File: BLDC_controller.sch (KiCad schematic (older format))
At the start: 77 parts, among them P1 CONN_01X02, P2 CONN_01X04, P3 CONN_01X02, P4 CONN_01X03, Q1 PSMN2R0-30YLD, Q2 PSMN2R0-30YLD, Q3 PSMN2R0-30YLD, Q4 PSMN2R0-30YLD, Q5 PSMN2R0-30YLD, Q6 PSMN2R0-30YLD

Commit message: add HALL header
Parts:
- added C18, C19: 220u, symbol CP
- added C20: 22u, symbol CP
- added C21: 10u, symbol CP
- added C22, C23, C24: 10p, symbol C
- added P5: CONN_01X05, symbol CONN_01X05
- added R40: 2k2, project_footprints:R_0603, symbol R
- added R41, R42, R43: 1k0, symbol R
- added R44, R45, R46: 10k, symbol R
- added V10: LED_ALT, symbol LED_ALT
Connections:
- wire segments 218 -> 257
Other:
- moved on the sheet: C15, C17, C7, L1, P1, R36, R37, R38, V8, V9

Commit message: minor change
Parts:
- removed C21: 10u, symbol CP
- removed P3: CONN_01X02, symbol CONN_01X02
- added P?: CONN_01X03, symbol CONN_01X03
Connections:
- wire segments 257 -> 252
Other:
- moved on the sheet: C10, C11, C12, C22, C23, C24, C9, P5, R17, R18, R19, R20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

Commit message: minor corrections
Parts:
- removed P2: CONN_01X04, symbol CONN_01X04
- added P2: CONN_01X06, symbol CONN_01X06
- added R47, R48, R49, R50: 1k0, project_footprints:R_0603, symbol R
- C22, C23, C24: footprint (none) -> project_footprints:C_0603
- R41, R42, R43, R44, R45, R46: footprint (none) -> project_footprints:R_0603
- gave numbers to parts that had none: 1
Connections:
- net labels added: 12V_FB, FP0, FP1, HALL1/A+, HALL2/B+, HALL3/Z+, I2C_SCL, I2C_SDA, NRST, OC_COMP, SW, SWCLK, SWDIO
- net labels removed: UART1_RX, UART1_TX
- wire segments 252 -> 259
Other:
- note added: "Digital\nHALL sensors"
- note added: "FP[1:0] determines \nA[1:0] of the I2C address"
- note added: "ST-LINK"
- moved on the sheet: C1, C10, C11, C12, C13, C14, C15, C16, C17, C18, C19, C2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

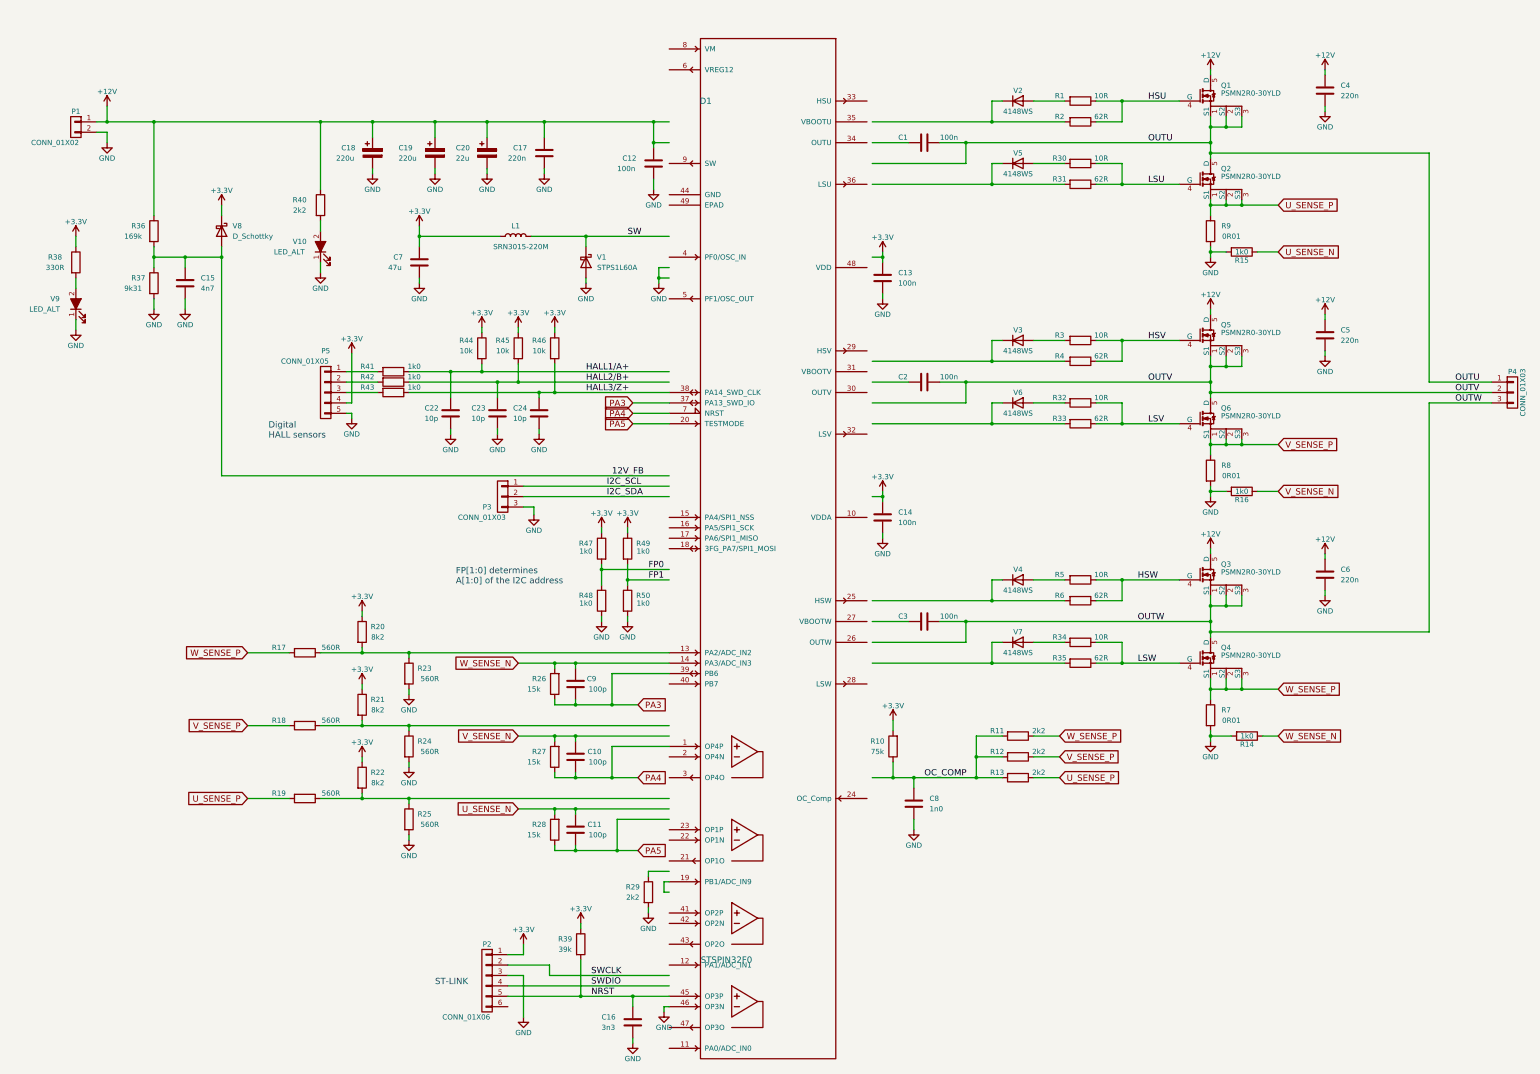
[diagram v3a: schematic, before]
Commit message: add SPI interface
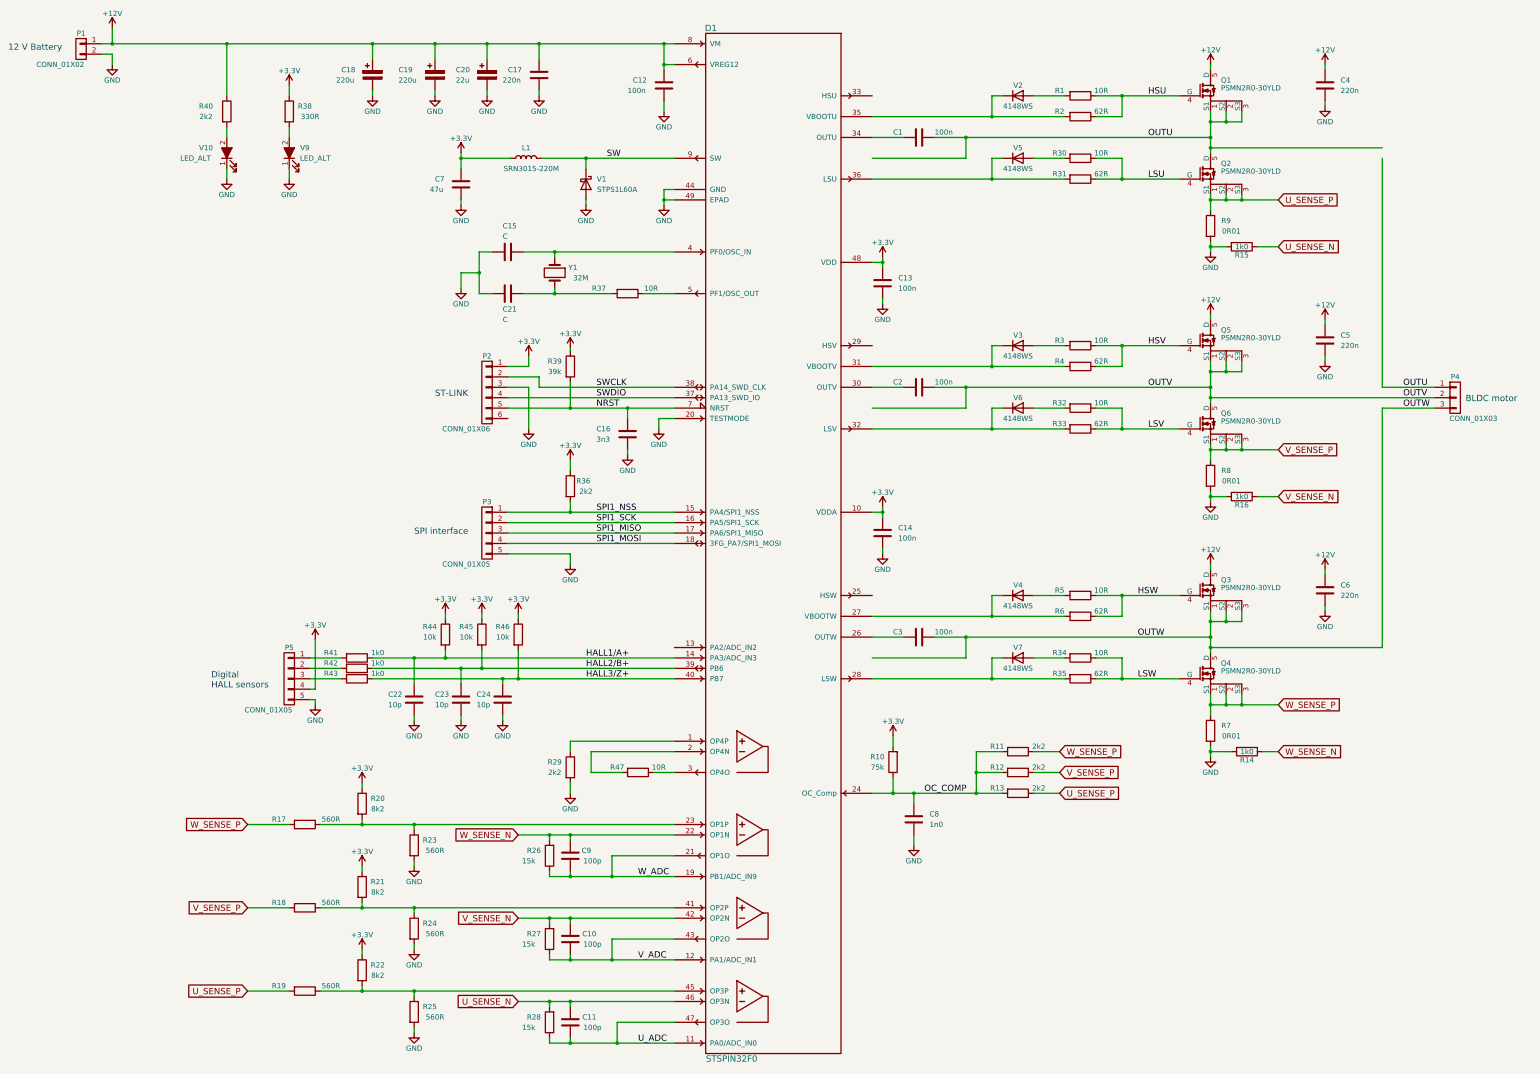
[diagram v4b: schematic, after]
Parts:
- removed P3: CONN_01X03, symbol CONN_01X03
- removed R48, R49, R50: 1k0, project_footprints:R_0603, symbol R
- removed V8: D_Schottky, symbol D_Schottky
- added C21: C, symbol C
- added P3: CONN_01X05, symbol CONN_01X05
- added Y1: 32M, symbol Crystal
- C15: value 4n7 -> C; footprint project_footprints:C_0603 -> (none)
- R36: value 169k -> 2k2; footprint project_footprints:R_0603 -> (none)
- R37: value 9k31 -> 10R; footprint project_footprints:R_0603 -> (none)
- R47: value 1k0 -> 10R
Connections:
- net labels added: SPI1_MISO, SPI1_MOSI, SPI1_NSS, SPI1_SCK, U_ADC, V_ADC, W_ADC
- net labels removed: 12V_FB, FP0, FP1, I2C_SCL, I2C_SDA, PA3, PA4, PA5
- wire segments 259 -> 254
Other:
- note added: "12 V Battery"
- note added: "BLDC motor"
- note added: "SPI interface"
- note removed: "FP[1:0] determines \nA[1:0] of the I2C address"
- moved on the sheet: C1, C10, C11, C12, C13, C14, C16, C17, C18, C19, C2, C20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

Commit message: cosmetic changes
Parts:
- C15, C21, R37: footprint (none) -> project_footprints:C_0603
- R36: footprint (none) -> project_footprints:R_0603
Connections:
- net OUTU: now also D1.34 (OUTU)
- net OUTV: now also D1.30 (OUTV)
- net OUTW: now also D1.26 (OUTW)
- net at D1.25 (HSW): now also R6.2, V4.1 (K)
- net at C3.2: now also D1.27 (VBOOTW); no longer D1.26 (OUTW)
- net at D1.29 (HSV): now also R4.2, V3.1 (K)
- net at C2.2: now also D1.31 (VBOOTV); no longer D1.30 (OUTV)
- net at D1.33 (HSU): now also R2.2, V2.1 (K)
- net at C1.2: now also D1.35 (VBOOTU); no longer D1.34 (OUTU)
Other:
- note added: "2816: 2 W @ +70 C"
- note added: "AN4999 Application note - STSPIN32F0 overcurrent protection:\n\nOC_TH_STBY2 (PF6) = 0\nOC_TH_STBY1 (PF7) = 1\nOC_SEL (PA11) = 1\nOC threshold = 100 mV"
- moved on the sheet: C1, C2, C3, C4, C5, C6, Q1, Q2, Q3, Q4, Q5, Q6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

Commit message: overcurrent protection documented
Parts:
- R10: value 75k -> 46k4
- R7, R8, R9: footprint project_footprints:R_2816 -> project_footprints:R_2512
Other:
- note added: "15 A current through a sense resistor causes 2.25 W heat dissipation. \nHowever, none of the three sense resistor conducts 100% of the time."
- note added: "AN2868 Application note - Oscillator design guide for STM32"
- note added: "AN4999 Application note - STSPIN32F0 overcurrent protection:\n\nOC_TH_STBY2 (PF6) = 0\nOC_TH_STBY1 (PF7) = 1\nOC_SEL (PA11) = 1\nOC threshold = 100 mV\n\nImax = 14.6 A => R10 = 46k4\n\nC8 = 1 nF => f_LP = 220 kHz\nwhich is about 5.5 times the switching frequency\n"
- note added: "Bourns CRA2512-FZ-R010ELF\n2512: 3 W @ +70 C"
- note removed: "2816: 2 W @ +70 C"
- note removed: "AN4999 Application note - STSPIN32F0 overcurrent protection:\n\nOC_TH_STBY2 (PF6) = 0\nOC_TH_STBY1 (PF7) = 1\nOC_SEL (PA11) = 1\nOC threshold = 100 mV"

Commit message: most footprints selected
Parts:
- removed Y1: 32M, symbol Crystal
- added G1: NX3225GD, project_footprints:Crystal_3225, symbol Crystal
- C18, C19: footprint (none) -> project_footprints:C_Radial_D10_L25_P5
- P2: footprint (none) -> project_footprints:PINHEAD1-6
- P3, P5: footprint (none) -> project_footprints:PINHEAD1-5
- V10, V9: footprint (none) -> project_footprints:LED_0402
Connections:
- net OSC_IN: now reaches C15.1, D1.4 (PF0/OSC_IN)
- net OSC_IN: now also G1.1
- net at C21.1, R37.2: now also G1.2
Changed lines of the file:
@@
 Sheet 1 1
 Title "BLDC CONTROLLER"
-Date "18.02.2017"
+Date "19.02.2017"
 Rev "0.2"
 Comp "Helsinki Hacklab"
@@
 F 0 "V9" V 3750 2000 50  0000 C CNN
 F 1 "LED_ALT" V 3650 1900 50  0000 C CNN
-F 2 "" H 3700 2150 50  0001 C CNN
+F 2 "project_footprints:LED_0402" H 3700 2150 50  0001 C CNN
 F 3 "" H 3700 2150 50  0000 C CNN
 	1    3700 2150
@@
 F 0 "C18" H 4200 1450 50  0000 L CNN
 F 1 "220u" H 4150 1350 50  0000 L CNN
-F 2 "" H 4538 1250 50  0001 C CNN
+F 2 "project_footprints:C_Radial_D10_L25_P5" H 4538 1250 50  0001 C CNN
 F 3 "" H 4500 1400 50  0000 C CNN
 	1    4500 1400
@@
 F 0 "C19" H 4750 1450 50  0000 L CNN
 F 1 "220u" H 4750 1350 50  0000 L CNN
-F 2 "" H 5138 1250 50  0001 C CNN
+F 2 "project_footprints:C_Radial_D10_L25_P5" H 5138 1250 50  0001 C CNN
 F 3 "" H 5100 1400 50  0000 C CNN
 	1    5100 1400
@@
 F 0 "V10" V 3150 2350 50  0000 C CNN
 F 1 "LED_ALT" V 3050 2450 50  0000 C CNN
-F 2 "" H 3100 2150 50  0001 C CNN
+F 2 "project_footprints:LED_0402" H 3100 2150 50  0001 C CNN
 F 3 "" H 3100 2150 50  0000 C CNN
 	1    3100 2150
@@
 F 0 "P5" H 3700 7500 50  0000 C CNN
 F 1 "CONN_01X05" H 3900 6900 50  0000 C CNN
-F 2 "" H 3700 7200 50  0001 C CNN
+F 2 "project_footprints:PINHEAD1-5" H 3700 7200 50  0001 C CNN
 F 3 "" H 3700 7200 50  0000 C CNN
 	1    3700 7200
@@
 F 0 "P2" H 5600 4800 50  0000 C CNN
 F 1 "CONN_01X06" H 5800 4100 50  0000 C CNN
-F 2 "" H 5600 4450 50  0001 C CNN
+F 2 "project_footprints:PINHEAD1-6" H 5600 4450 50  0001 C CNN
 F 3 "" H 5600 4450 50  0000 C CNN
 	1    5600 4450
@@
 	1    0    0    -1
 $EndComp
-$Comp
-L Crystal Y1
-U 1 1 58AA45EE
-P 6250 3300
-F 0 "Y1" V 6200 3475 50  0000 C CNN
-F 1 "32M" V 6300 3550 50  0000 C CNN
-F 2 "" H 6250 3300 50  0001 C CNN
-F 3 "" H 6250 3300 50  0000 C CNN
-	1    6250 3300
-	0    1    1    0
-$EndComp
 Wire Wire Line
 	6250 3150 6250 3100
@@
 F 0 "P3" H 5600 6100 50  0000 C CNN
 F 1 "CONN_01X05" H 5800 5500 50  0000 C CNN
-F 2 "" H 5600 5800 50  0001 C CNN
+F 2 "project_footprints:PINHEAD1-5" H 5600 5800 50  0001 C CNN
 F 3 "" H 5600 5800 50  0000 C CNN
 	1    5600 5800
@@
 Text Notes 2150 3200 0    60   ~ 0
 AN2868 Application note - Oscillator design guide for STM32
+Text Label 6800 3100 0    60   ~ 0
+OSC_IN
+$Comp
+L Crystal G1
+U 1 1 58AD39C7
+P 6250 3300
+F 0 "G1" V 6200 3500 50  0000 C CNN
+F 1 "NX3225GD" V 6300 3650 50  0000 C CNN
+F 2 "project_footprints:Crystal_3225" H 6250 3300 50  0001 C CNN
+F 3 "" H 6250 3300 50  0000 C CNN
+	1    6250 3300
+	0    1    1    0
+$EndComp
 $EndSCHEMATC

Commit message: parts in place
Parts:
- removed C19: 220u, project_footprints:C_Radial_D10_L25_P5, symbol CP
- removed C20: 22u, symbol CP
- added C19, C20, C25, C26, C27: 220n, project_footprints:C_0805, symbol C
- C10, C11, C15, C16, C21, C22, C23, C24, C8, C9: footprint project_footprints:C_0603 -> project_footprints:C_0402
- C18: value 220u -> 680u
- R1, R2, R3, R30, R31, R32, R33, R34, R35, R4, R40, R5, R6: footprint project_footprints:R_0603 -> project_footprints:R_0603_NOM
- R10, R11, R12, R13, R14, R15, R16, R17, R18, R19, R20, R21, R22, R23, R24, R25, R26, R27, R28, R29, R36, R38, R39, R41, R42, R43, R44, R45, R46, R47: footprint project_footprints:R_0603 -> project_footprints:R_0402_MOST
- R37: footprint project_footprints:C_0603 -> project_footprints:R_0402_MOST
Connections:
- net +12V: now also C19.1, C20.1, C25.1, C26.1, C27.1
- net GND: now also C19.2, C20.2, C25.2, C26.2, C27.2
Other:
- moved on the sheet: C4, C5, C6, P4
